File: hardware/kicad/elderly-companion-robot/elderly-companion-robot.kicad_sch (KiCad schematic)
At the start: 6 parts

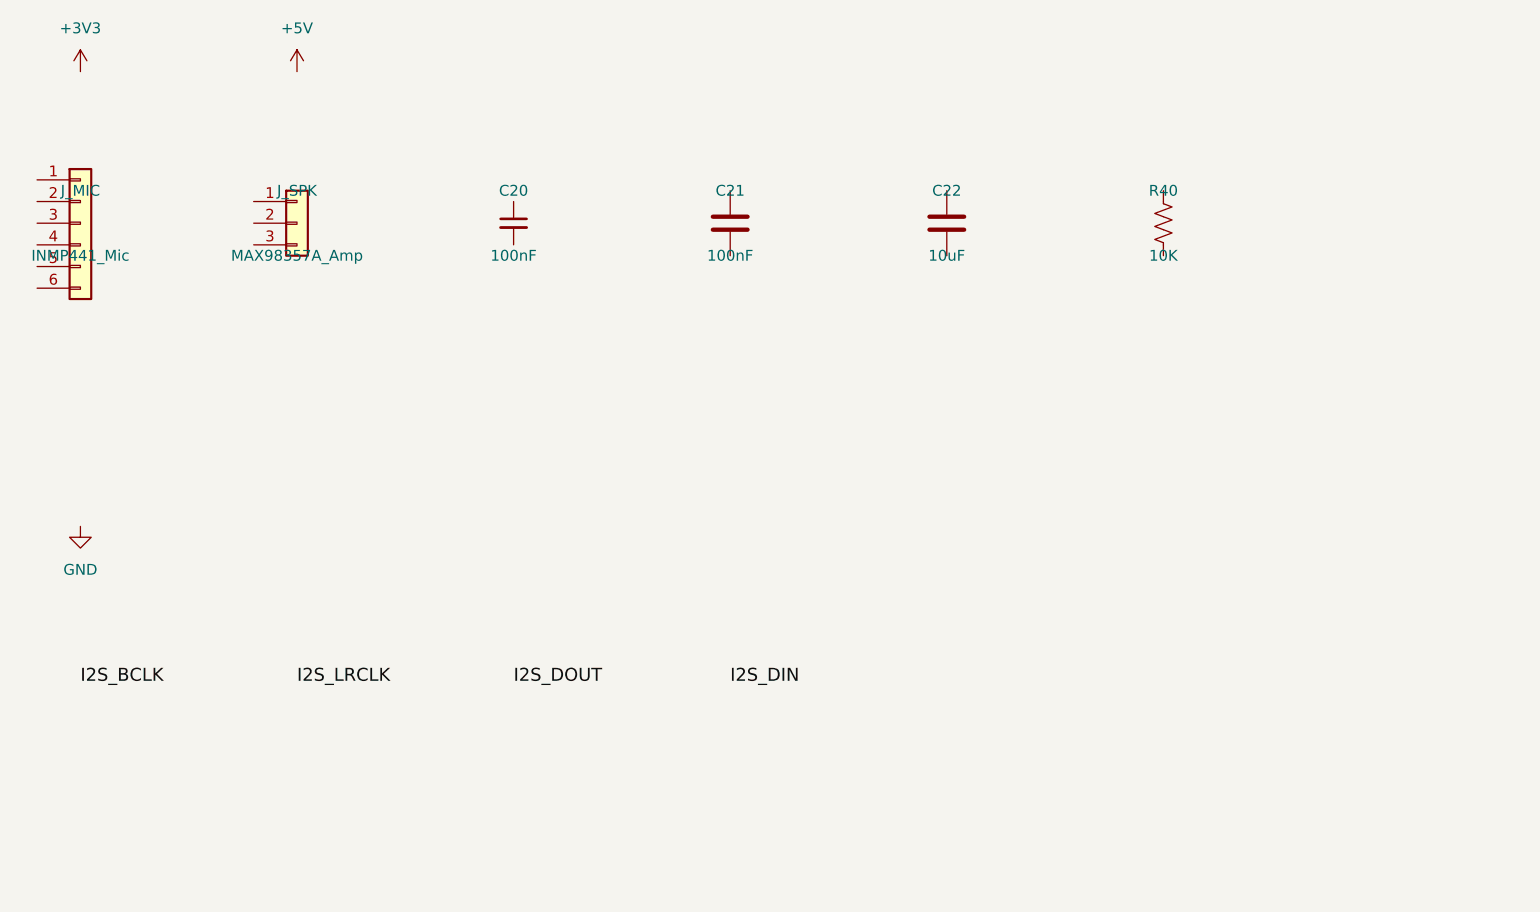
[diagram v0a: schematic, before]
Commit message: Phase 9 WIP: Camera/Dock + SIM800L sheet — servos, IR, dock, SIM800L
- 2x SG90 servo connectors (J_SERVO1 Pan, J_SERVO2 Tilt)
- IR beacon connector (J_IR) with 220R series resistor (R50)
- Dock contact connector (J_DOCK)
- ESP32-S3-CAM connector (J_CAM, 4-pin)
- SIM800C/SIM800L module (U_SIM) — using SIM800C symbol as proxy
- SIM800L bypass caps: C30 100uF, C31 100nF
- Hierarchical labels: SERVO_PAN, SERVO_TILT, IR_TX, IR_RX,
  SIM800L_TX, SIM800L_RX, SIM800L_PWRKEY
- Power: +5V (servos, IR, CAM), +4V (SIM800L), +3V3, GND

Co-Authored-By: Claude Opus 4.7 <noreply@anthropic.com>
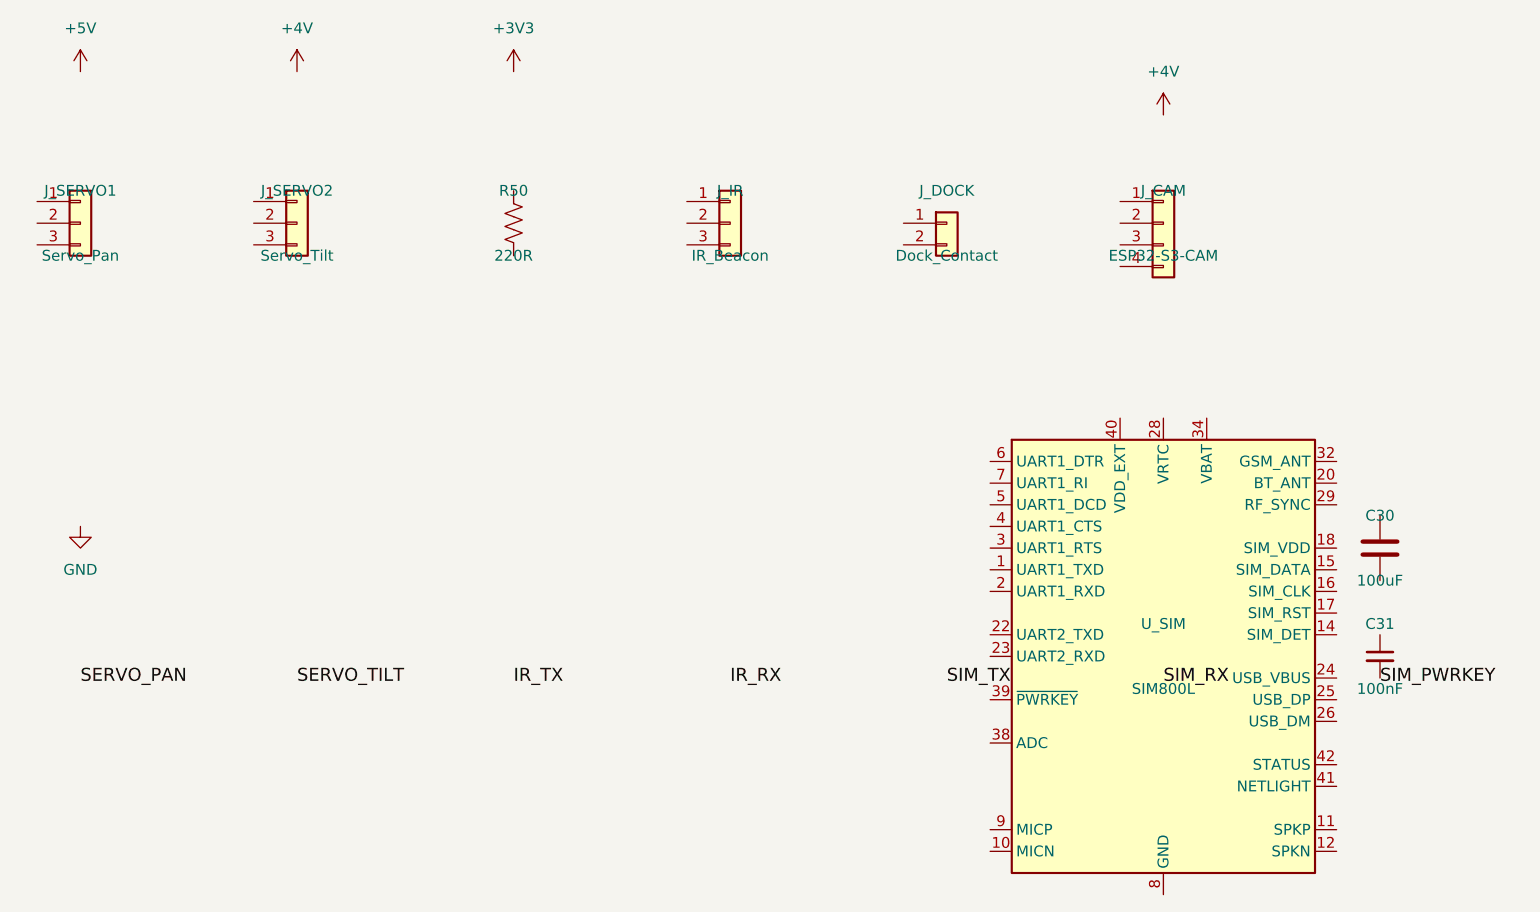
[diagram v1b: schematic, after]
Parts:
- removed C20: 100nF, symbol Device:C_Small
- removed C21: 100nF, symbol Device:C
- removed C22: 10uF, symbol Device:C
- removed J_MIC: INMP441_Mic, symbol Connector_Generic:Conn_01x06
- removed J_SPK: MAX98357A_Amp, symbol Connector_Generic:Conn_01x03
- removed R40: 10K, symbol Device:R_US
- added C30: 100uF, symbol Device:C
- added C31: 100nF, symbol Device:C_Small
- added J_CAM: ESP32-S3-CAM, symbol Connector_Generic:Conn_01x04
- added J_DOCK: Dock_Contact, symbol Connector_Generic:Conn_01x02
- added J_IR: IR_Beacon, symbol Connector_Generic:Conn_01x03
- added J_SERVO1: Servo_Pan, symbol Connector_Generic:Conn_01x03
- added J_SERVO2: Servo_Tilt, symbol Connector_Generic:Conn_01x03
- added R50: 220R, symbol Device:R_US
- added U_SIM: SIM800L, symbol RF_GSM:SIM800C
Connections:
- new net: U_SIM.13 (GND), U_SIM.19 (GND), U_SIM.21 (GND), U_SIM.27 (GND), U_SIM.30 (GND), U_SIM.31 (GND), U_SIM.33 (GND), U_SIM.36 (GND), U_SIM.37 (GND), U_SIM.8 (GND)
- new net: U_SIM.34 (VBAT), U_SIM.35 (VBAT)
- new net SIM_PWRKEY: C31.2
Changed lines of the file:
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@@
 	(paper "A4")
 	(symbol
-		(lib_id "Connector_Generic:Conn_01x06")
+		(lib_id "Connector_Generic:Conn_01x03")
 		(at 50.8 50.8 0)
 		(unit 1)
@@
 		(on_board yes)
 		(dnp no)
-		(property "Reference" "J_MIC"
+		(property "Reference" "J_SERVO1"
 			(at 50.8 46.99 0)
 			(effects (font (size 1.27 1.27)))
 		)
-		(property "Value" "INMP441_Mic"
+		(property "Value" "Servo_Pan"
 			(at 50.8 54.61 0)
 			(effects (font (size 1.27 1.27)))
@@
 		(instances
 			(project "elderly-companion-robot"
-				(path "/abd534f8-9c28-4628-93df-4a5faa112927"
-					(reference "J_MIC") (unit 1)
+				(path "/8a09b215-3de3-42dd-ba8d-6891067f794f"
+					(reference "J_SERVO1") (unit 1)
 				)
 			)
@@
 		(on_board yes)
 		(dnp no)
-		(property "Reference" "J_SPK"
+		(property "Reference" "J_SERVO2"
 			(at 76.2 46.99 0)
 			(effects (font (size 1.27 1.27)))
 		)
-		(property "Value" "MAX98357A_Amp"
+		(property "Value" "Servo_Tilt"
 			(at 76.2 54.61 0)
 			(effects (font (size 1.27 1.27)))
@@
 		(instances
 			(project "elderly-companion-robot"
-				(path "/abd534f8-9c28-4628-93df-4a5faa112927"
-					(reference "J_SPK") (unit 1)
-				)
-			)
-		)
-	)
-	(symbol
-		(lib_id "Device:C_Small")
+				(path "/8a09b215-3de3-42dd-ba8d-6891067f794f"
+					(reference "J_SERVO2") (unit 1)
+				)
+			)
+		)
+	)
+	(symbol
+		(lib_id "Device:R_US")
 		(at 101.6 50.8 0)
 		(unit 1)
@@
 		(on_board yes)
 		(dnp no)
-		(property "Reference" "C20"
+		(property "Reference" "R50"
 			(at 101.6 46.99 0)
 			(effects (font (size 1.27 1.27)))
 		)
-		(property "Value" "100nF"
+		(property "Value" "220R"
 			(at 101.6 54.61 0)
 			(effects (font (size 1.27 1.27)))
@@
 		(instances
 			(project "elderly-companion-robot"
-				(path "/abd534f8-9c28-4628-93df-4a5faa112927"
-					(reference "C20") (unit 1)
-				)
-			)
-		)
-	)
-	(symbol
-		(lib_id "Device:C")
+				(path "/8a09b215-3de3-42dd-ba8d-6891067f794f"
+					(reference "R50") (unit 1)
+				)
+			)
+		)
+	)
+	(symbol
+		(lib_id "Connector_Generic:Conn_01x03")
 		(at 127 50.8 0)
 		(unit 1)
@@
 		(on_board yes)
 		(dnp no)
-		(property "Reference" "C21"
+		(property "Reference" "J_IR"
 			(at 127 46.99 0)
 			(effects (font (size 1.27 1.27)))
 		)
-		(property "Value" "100nF"
+		(property "Value" "IR_Beacon"
 			(at 127 54.61 0)
 			(effects (font (size 1.27 1.27)))
@@
 		(instances
 			(project "elderly-companion-robot"
-				(path "/abd534f8-9c28-4628-93df-4a5faa112927"
-					(reference "C21") (unit 1)
-				)
-			)
-		)
-	)
-	(symbol
-		(lib_id "Device:C")
+				(path "/8a09b215-3de3-42dd-ba8d-6891067f794f"
+					(reference "J_IR") (unit 1)
+				)
+			)
+		)
+	)
+	(symbol
+		(lib_id "Connector_Generic:Conn_01x02")
 		(at 152.4 50.8 0)
 		(unit 1)
@@
 		(on_board yes)
 		(dnp no)
-		(property "Reference" "C22"
+		(property "Reference" "J_DOCK"
 			(at 152.4 46.99 0)
 			(effects (font (size 1.27 1.27)))
 		)
-		(property "Value" "10uF"
+		(property "Value" "Dock_Contact"
 			(at 152.4 54.61 0)
 			(effects (font (size 1.27 1.27)))
@@
 		(instances
 			(project "elderly-companion-robot"
-				(path "/abd534f8-9c28-4628-93df-4a5faa112927"
-					(reference "C22") (unit 1)
-				)
-			)
-		)
-	)
-	(symbol
-		(lib_id "Device:R_US")
+				(path "/8a09b215-3de3-42dd-ba8d-6891067f794f"
+					(reference "J_DOCK") (unit 1)
+				)
+			)
+		)
+	)
+	(symbol
+		(lib_id "Connector_Generic:Conn_01x04")
 		(at 177.8 50.8 0)
 		(unit 1)
@@
 		(on_board yes)
 		(dnp no)
-		(property "Reference" "R40"
+		(property "Reference" "J_CAM"
 			(at 177.8 46.99 0)
 			(effects (font (size 1.27 1.27)))
 		)
-		(property "Value" "10K"
+		(property "Value" "ESP32-S3-CAM"
 			(at 177.8 54.61 0)
 			(effects (font (size 1.27 1.27)))
@@
 		(instances
 			(project "elderly-companion-robot"
-				(path "/abd534f8-9c28-4628-93df-4a5faa112927"
-					(reference "R40") (unit 1)
-				)
-			)
-		)
-	)
-	(symbol
-		(lib_id "power:+3V3")
+				(path "/8a09b215-3de3-42dd-ba8d-6891067f794f"
+					(reference "J_CAM") (unit 1)
+				)
+			)
+		)
+	)
+	(symbol
+		(lib_id "power:+5V")
 		(at 50.8 33.02 0)
 		(unit 1)
@@
 			(effects (font (size 1.27 1.27)) (hide yes))
 		)
-		(property "Value" "+3V3"
+		(property "Value" "+5V"
 			(at 50.8 27.94 0)
 			(effects (font (size 1.27 1.27)))
@@
 		(instances
 			(project "elderly-companion-robot"
-				(path "/abd534f8-9c28-4628-93df-4a5faa112927"
+				(path "/8a09b215-3de3-42dd-ba8d-6891067f794f"
 					(reference "#PWR001") (unit 1)
 				)
@@
 	)
 	(symbol
-		(lib_id "power:+5V")
+		(lib_id "power:+4V")
 		(at 76.2 33.02 0)
 		(unit 1)
@@
 			(effects (font (size 1.27 1.27)) (hide yes))
 		)
-		(property "Value" "+5V"
+		(property "Value" "+4V"
 			(at 76.2 27.94 0)
 			(effects (font (size 1.27 1.27)))
@@
 		(instances
 			(project "elderly-companion-robot"
-				(path "/abd534f8-9c28-4628-93df-4a5faa112927"
+				(path "/8a09b215-3de3-42dd-ba8d-6891067f794f"
 					(reference "#PWR002") (unit 1)
+				)
+			)
+		)
+	)
+	(symbol
+		(lib_id "power:+3V3")
+		(at 101.6 33.02 0)
+		(unit 1)
+		(exclude_from_sim no)
+		(in_bom yes)
+		(on_board yes)
+		(dnp no)
+		(property "Reference" "#PWR003"
+			(at 101.6 26.67 0)
+			(effects (font (size 1.27 1.27)) (hide yes))
+		)
+		(property "Value" "+3V3"
+			(at 101.6 27.94 0)
+			(effects (font (size 1.27 1.27)))
+		)
+		(property "Footprint" ""
+			(at 101.6 33.02 0)
+			(effects (font (size 1.27 1.27)) (hide yes))
+		)
+		(property "Datasheet" "~"
+			(at 101.6 33.02 0)
+			(effects (font (size 1.27 1.27)) (hide yes))
+		)
+		(instances
+			(project "elderly-companion-robot"
+				(path "/8a09b215-3de3-42dd-ba8d-6891067f794f"
+					(reference "#PWR003") (unit 1)
 				)
 			)
@@
 		(on_board yes)
 		(dnp no)
-		(property "Reference" "#PWR003"
+		(property "Reference" "#PWR004"
 			(at 50.8 92.71 0)
 			(effects (font (size 1.27 1.27)) (hide yes))
@@
 		(instances
 			(project "elderly-companion-robot"
-				(path "/abd534f8-9c28-4628-93df-4a5faa112927"
-					(reference "#PWR003") (unit 1)
-				)
-			)
-		)
-	)
-	(label "I2S_BCLK"
+				(path "/8a09b215-3de3-42dd-ba8d-6891067f794f"
+					(reference "#PWR004") (unit 1)
+				)
+			)
+		)
+	)
+	(label "SERVO_PAN"
 		(at 50.8 104.14 0)
 		(effects (font (size 1.524 1.524)))
 	)
-	(label "I2S_LRCLK"
+	(label "SERVO_TILT"
 		(at 76.2 104.14 0)
 		(effects (font (size 1.524 1.524)))
 	)
-	(label "I2S_DOUT"
+	(label "IR_TX"
 		(at 101.6 104.14 0)
 		(effects (font (size 1.524 1.524)))
 	)
-	(label "I2S_DIN"
+	(label "IR_RX"
 		(at 127 104.14 0)
 		(effects (font (size 1.524 1.524)))
 	)
+	(label "SIM_TX"
+		(at 152.4 104.14 0)
+		(effects (font (size 1.524 1.524)))
+	)
+	(label "SIM_RX"
+		(at 177.8 104.14 0)
+		(effects (font (size 1.524 1.524)))
+	)
+	(label "SIM_PWRKEY"
+		(at 203.2 104.14 0)
+		(effects (font (size 1.524 1.524)))
+	)
+	(symbol
+		(lib_id "Device:C")
+		(at 203.2 88.9 0)
+		(unit 1)
+		(exclude_from_sim no)
+		(in_bom yes)
+		(on_board yes)
+		(dnp no)
+		(property "Reference" "C30"
+			(at 203.2 85.09 0)
+			(effects (font (size 1.27 1.27)))
+		)
+		(property "Value" "100uF"
+			(at 203.2 92.71 0)
+			(effects (font (size 1.27 1.27)))
+		)
+		(property "Footprint" ""
+			(at 203.2 88.9 0)
+			(effects (font (size 1.27 1.27)) (hide yes))
+		)
+		(property "Datasheet" "~"
+			(at 203.2 88.9 0)
+			(effects (font (size 1.27 1.27)) (hide yes))
+		)
+		(instances
+			(project "elderly-companion-robot"
+				(path "/e13f87b0-27dd-42ef-91fe-f82e5360fa44"
+					(reference "C30") (unit 1)
+				)
+			)
+		)
+	)
+	(symbol
+		(lib_id "Device:C_Small")
+		(at 203.2 101.6 0)
+		(unit 1)
+		(exclude_from_sim no)
+		(in_bom yes)
+		(on_board yes)
+		(dnp no)
+		(property "Reference" "C31"
+			(at 203.2 97.79 0)
+			(effects (font (size 1.27 1.27)))
+		)
+		(property "Value" "100nF"
+			(at 203.2 105.41 0)
+			(effects (font (size 1.27 1.27)))
+		)
+		(property "Footprint" ""
+			(at 203.2 101.6 0)
+			(effects (font (size 1.27 1.27)) (hide yes))
+		)
+		(property "Datasheet" "~"
+			(at 203.2 101.6 0)
+			(effects (font (size 1.27 1.27)) (hide yes))
+		)
+		(instances
+			(project "elderly-companion-robot"
+				(path "/72891e2a-8a06-48c8-90e8-c6ad2c013135"
+					(reference "C31") (unit 1)
+				)
+			)
+		)
+	)
+	(symbol
+		(lib_id "RF_GSM:SIM800C")
+		(at 177.8 101.6 0)
+		(unit 1)
+		(exclude_from_sim no)
+		(in_bom yes)
+		(on_board yes)
+		(dnp no)
+		(property "Reference" "U_SIM"
+			(at 177.8 97.79 0)
+			(effects (font (size 1.27 1.27)))
+		)
+		(property "Value" "SIM800L"
+			(at 177.8 105.41 0)
+			(effects (font (size 1.27 1.27)))
+		)
+		(property "Footprint" ""
+			(at 177.8 101.6 0)
+			(effects (font (size 1.27 1.27)) (hide yes))
+		)
+		(property "Datasheet" "~"
+			(at 177.8 101.6 0)
+			(effects (font (size 1.27 1.27)) (hide yes))
+		)
+		(instances
+			(project "elderly-companion-robot"
+				(path "/4b57f1a5-7f7b-45c6-b12d-079ac16d580b"
+					(reference "U_SIM") (unit 1)
+				)
+			)
+		)
+	)
+	(symbol
+		(lib_id "power:+4V")
+		(at 177.8 38.1 0)
+		(unit 1)
+		(exclude_from_sim no)
+		(in_bom yes)
+		(on_board yes)
+		(dnp no)
+		(property "Reference" "#PWR4ec9"
+			(at 177.8 31.75 0)
+			(effects (font (size 1.27 1.27)) (hide yes))
+		)
+		(property "Value" "+4V"
+			(at 177.8 33.02 0)
+			(effects (font (size 1.27 1.27)))
+		)
+		(property "Footprint" ""
+			(at 177.8 38.1 0)
+			(effects (font (size 1.27 1.27)) (hide yes))
+		)
+		(property "Datasheet" "~"
+			(at 177.8 38.1 0)
+			(effects (font (size 1.27 1.27)) (hide yes))
+		)
+		(instances
+			(project "elderly-companion-robot"
+				(path "/7ea93241-9e2e-4257-be31-f5a1cb990cf5"
+					(reference "#PWR4ec9") (unit 1)
+				)
+			)
+		)
+	)
 	(sheet_instances
